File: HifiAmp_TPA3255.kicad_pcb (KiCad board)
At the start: 4 copper layers, 200 x 150 mm, 124 parts, among them J1 PVDD 48V IN — NEEDS_DATA, J2 RCA L SE, J3 RCA R SE, J301 SPK_L, J302 SPK_R, J4 VOLUME_REMOTE, Q301 IPP330P10NM, Q302 IXTK200N10L2, U1 LM5010ASD, U2 LM2940IMP-12/NOPB, U3 TLV1117-33IDCY, U4 OPA1612AIDR, U5 OPA1612AIDR, U6 TPA3255B, U7 TPS3802K33DCKR, U8 LM5069-2

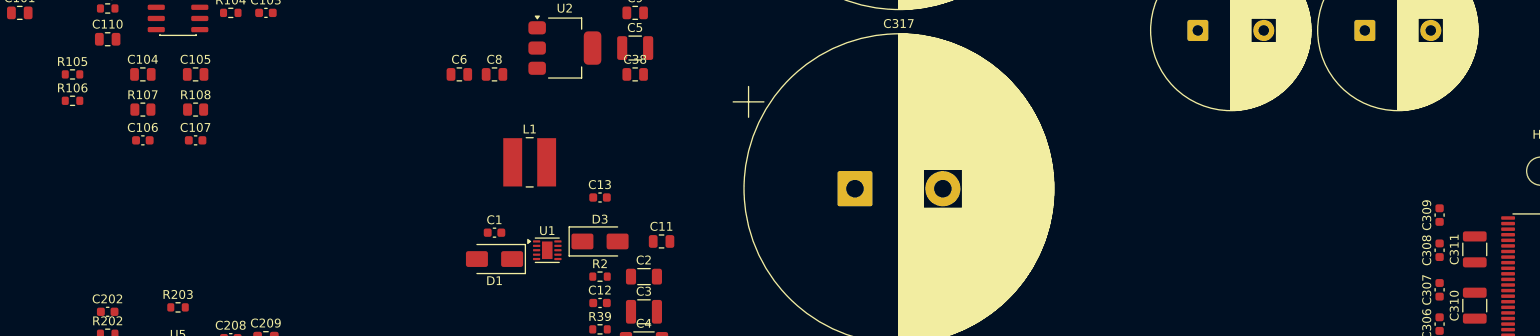
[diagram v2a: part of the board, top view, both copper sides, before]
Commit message: feat(e1.5): correct the two gratuitous asymmetries, and leave the third alone
The mirror around y=175 makes summed ordinates the criterion, not distance, so
C306 and C307 stay put and set the target their partners move to. C308, C309 and
C311 now sum to 350; R105/R106 keep the shared VMID divider but sit midway
between the channels, equalising both reference paths. The inductors' offset is
left as it is: the 2x2 grid is forced by the courtyard, and the mismatch leaves
as an F1 routing constraint instead.

Five IPC moves, all in y. DRC reads 105 violations, every one silkscreen, with
no clearance and no courtyards_overlap — which is what validates the tightest
3.0 mm pitch, since a hand-rolled courtyard calculation would only have proved
its own model. The 119 other footprints are untouched.

The previous session's GUI block is resolved and the escape route verified: the
SendInput block never reached the IPC, and did not survive the session.

Co-Authored-By: Claude Opus 5 <noreply@anthropic.com>
Claude-Session: https://claude.ai/code/session_017KEKgkQHHQWX4vViqUxNCh
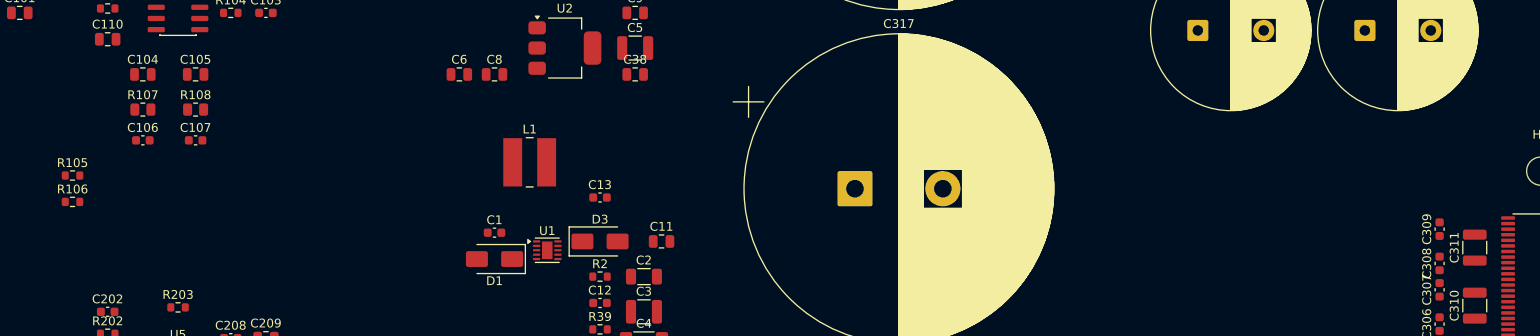
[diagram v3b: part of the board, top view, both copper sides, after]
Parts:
- moved R105 11.5 mm to (118.0, 163.5)
- moved R106 11.5 mm to (118.0, 166.5)
- moved C309 1.60 mm to (273.5, 169.6)
- moved C308 1.50 mm to (273.5, 173.5)
- moved C311 0.20 mm to (277.5, 171.7)
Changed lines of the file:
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@@
 	(footprint "Resistor_SMD:R_0603_1608Metric"
 		(layer "F.Cu")
-		(at 118 155)
+		(at 118 166.5)
 		(descr "Resistor SMD 0603 (1608 Metric), square (rectangular) end terminal, IPC-7351 nominal, (Body size source: IPC-SM-782 page 72, https://www.pcb-3d.com/wordpress/wp-content/uploads/ipc-sm-782a_amendment_1_and_2.pdf)")
 		(tags "resistor")
@@
 	(footprint "Capacitor_SMD:C_0603_1608Metric"
 		(layer "F.Cu")
-		(at 273.5 168 90)
+		(at 273.5 169.6 90)
 		(descr "Capacitor SMD 0603 (1608 Metric), square (rectangular) end terminal, IPC-7351 nominal, (Body size source: IPC-SM-782 page 76, https://www.pcb-3d.com/wordpress/wp-content/uploads/ipc-sm-782a_amendment_1_and_2.pdf)")
 		(tags "capacitor")
@@
 	(footprint "Resistor_SMD:R_0603_1608Metric"
 		(layer "F.Cu")
-		(at 118 152)
+		(at 118 163.5)
 		(descr "Resistor SMD 0603 (1608 Metric), square (rectangular) end terminal, IPC-7351 nominal, (Body size source: IPC-SM-782 page 72, https://www.pcb-3d.com/wordpress/wp-content/uploads/ipc-sm-782a_amendment_1_and_2.pdf)")
 		(tags "resistor")
@@
 	(footprint "Capacitor_SMD:C_0603_1608Metric"
 		(layer "F.Cu")
-		(at 273.5 172 90)
+		(at 273.5 173.5 90)
 		(descr "Capacitor SMD 0603 (1608 Metric), square (rectangular) end terminal, IPC-7351 nominal, (Body size source: IPC-SM-782 page 76, https://www.pcb-3d.com/wordpress/wp-content/uploads/ipc-sm-782a_amendment_1_and_2.pdf)")
 		(tags "capacitor")
@@
 	(footprint "Capacitor_SMD:C_1210_3225Metric"
 		(layer "F.Cu")
-		(at 277.5 171.9 90)
+		(at 277.5 171.7 90)
 		(descr "Capacitor SMD 1210 (3225 Metric), square (rectangular) end terminal, IPC-7351 nominal, (Body size source: IPC-SM-782 page 76, https://www.pcb-3d.com/wordpress/wp-content/uploads/ipc-sm-782a_amendment_1_and_2.pdf)")
 		(tags "capacitor")

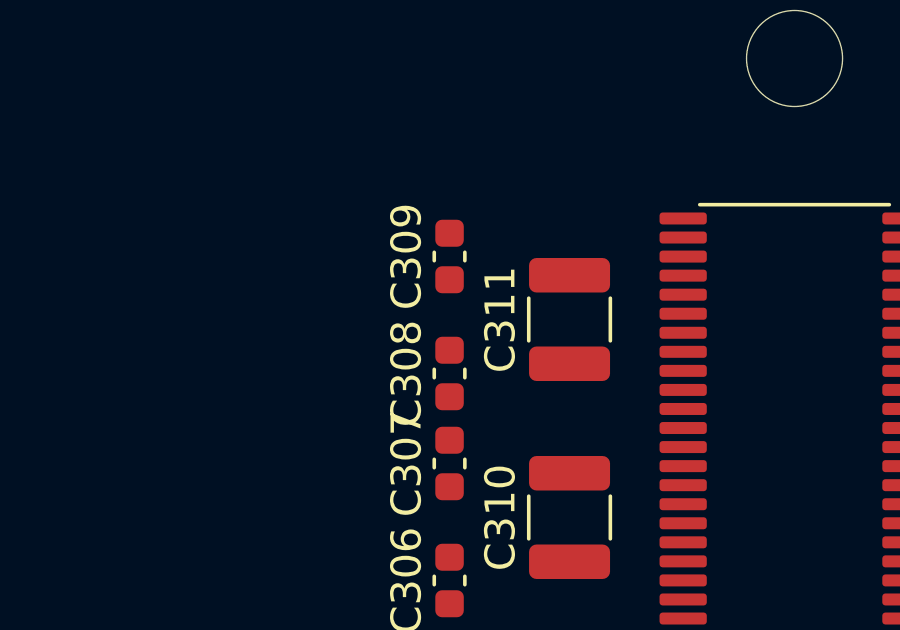
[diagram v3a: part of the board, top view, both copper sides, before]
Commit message: feat(e1.5): finish the mirror by rotating the two reversed bootstraps
C308 and C309 go from 90 to 270 degrees with no move at all: the centres stay
identical to the micron, so the sums to 350 from the corrective slice survive
untouched. C306 and C307 stay as they are — rotating them would cross them.

The crossing test replayed over the six capacitors around U6 now returns zero
crossings, so no bootstrap loop needs a via. DRC holds at silkscreen only, with
no clearance and no courtyards_overlap.

Worth knowing for later checks: the IPC writes this orientation as -90 rather
than 270. Equivalent modulo 360, but a check looking for the literal 270 would
report a failure that is not there.

Co-Authored-By: Claude Opus 5 <noreply@anthropic.com>
Claude-Session: https://claude.ai/code/session_017KEKgkQHHQWX4vViqUxNCh
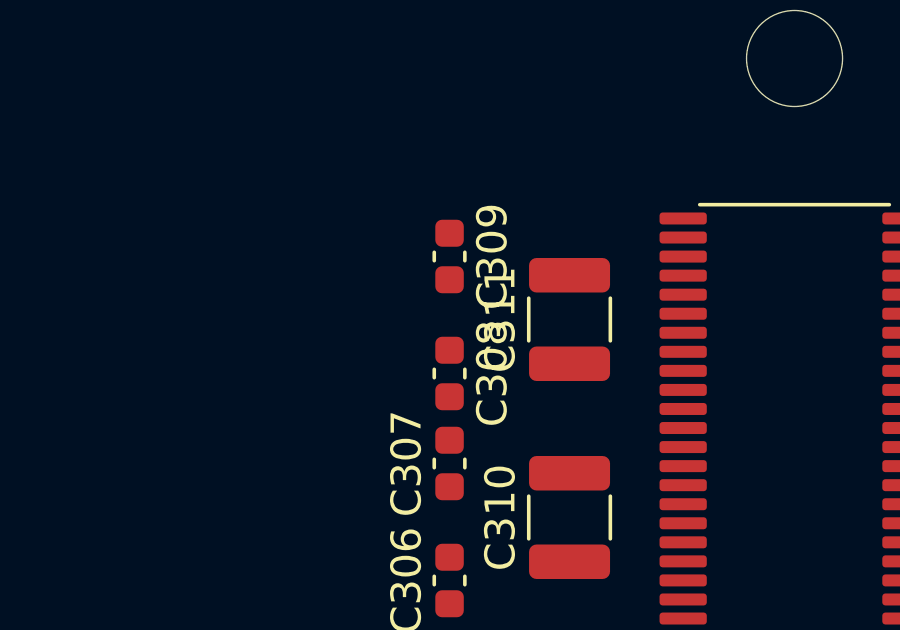
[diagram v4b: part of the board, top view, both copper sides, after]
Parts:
- turned C308 to -90 degrees
- turned C309 to -90 degrees
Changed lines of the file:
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@@
 	(footprint "Capacitor_SMD:C_0603_1608Metric"
 		(layer "F.Cu")
-		(at 273.5 169.6 90)
+		(at 273.5 169.6 -90)
 		(descr "Capacitor SMD 0603 (1608 Metric), square (rectangular) end terminal, IPC-7351 nominal, (Body size source: IPC-SM-782 page 76, https://www.pcb-3d.com/wordpress/wp-content/uploads/ipc-sm-782a_amendment_1_and_2.pdf)")
 		(tags "capacitor")
 		(property "Reference" "C309"
-			(at 0 -1.43 90)
+			(at 0 -1.43 -90)
 			(layer "F.SilkS")
 			(effects
@@
 		)
 		(property "Value" "0.033uF"
-			(at 0 1.43 90)
+			(at 0 1.43 -90)
 			(layer "F.Fab")
 			(effects
@@
 		)
 		(property "Datasheet" ""
-			(at 0 0 90)
+			(at 0 0 -90)
 			(layer "F.Fab")
 			(hide yes)
@@
 		)
 		(property "Description" ""
-			(at 0 0 90)
+			(at 0 0 -90)
 			(layer "F.Fab")
 			(hide yes)
@@
 		)
 		(property "KiLib_Generator" "SMD_2terminal_chip_molded"
-			(at 0 0 90)
+			(at 0 0 -90)
 			(layer "F.SilkS")
 			(hide yes)
@@
 		(duplicate_pad_numbers_are_jumpers no)
 		(fp_line
-			(start -0.14058 -0.51)
-			(end 0.14058 -0.51)
+			(start -0.14058 0.51)
+			(end 0.14058 0.51)
 			(stroke
 				(width 0.12)
@@
 		)
 		(fp_line
-			(start -0.14058 0.51)
-			(end 0.14058 0.51)
+			(start -0.14058 -0.51)
+			(end 0.14058 -0.51)
 			(stroke
 				(width 0.12)
@@
 		)
 		(fp_text user "${REFERENCE}"
-			(at 0 0 90)
+			(at 0 0 -90)
 			(layer "F.Fab")
 			(effects
@@
 		)
 		(pad "1" smd roundrect
-			(at -0.775 0 90)
+			(at -0.775 0 270)
 			(size 0.9 0.95)
 			(layers "F.Cu" "F.Mask" "F.Paste")
@@
 		)
 		(pad "2" smd roundrect
-			(at 0.775 0 90)
+			(at 0.775 0 270)
 			(size 0.9 0.95)
 			(layers "F.Cu" "F.Mask" "F.Paste")
@@
 	(footprint "Capacitor_SMD:C_0603_1608Metric"
 		(layer "F.Cu")
-		(at 273.5 173.5 90)
+		(at 273.5 173.5 -90)
 		(descr "Capacitor SMD 0603 (1608 Metric), square (rectangular) end terminal, IPC-7351 nominal, (Body size source: IPC-SM-782 page 76, https://www.pcb-3d.com/wordpress/wp-content/uploads/ipc-sm-782a_amendment_1_and_2.pdf)")
 		(tags "capacitor")
 		(property "Reference" "C308"
-			(at 0 -1.43 90)
+			(at 0 -1.43 -90)
 			(layer "F.SilkS")
 			(effects
@@
 		)
 		(property "Value" "0.033uF"
-			(at 0 1.43 90)
+			(at 0 1.43 -90)
 			(layer "F.Fab")
 			(effects
@@
 		)
 		(property "Datasheet" ""
-			(at 0 0 90)
+			(at 0 0 -90)
 			(layer "F.Fab")
 			(hide yes)
@@
 		)
 		(property "Description" ""
-			(at 0 0 90)
+			(at 0 0 -90)
 			(layer "F.Fab")
 			(hide yes)
@@
 		)
 		(property "KiLib_Generator" "SMD_2terminal_chip_molded"
-			(at 0 0 90)
+			(at 0 0 -90)
 			(layer "F.SilkS")
 			(hide yes)
@@
 		(duplicate_pad_numbers_are_jumpers no)
 		(fp_line
-			(start -0.14058 -0.51)
-			(end 0.14058 -0.51)
+			(start -0.14058 0.51)
+			(end 0.14058 0.51)
 			(stroke
 				(width 0.12)
@@
 		)
 		(fp_line
-			(start -0.14058 0.51)
-			(end 0.14058 0.51)
+			(start -0.14058 -0.51)
+			(end 0.14058 -0.51)
 			(stroke
 				(width 0.12)
@@
 		)
 		(fp_text user "${REFERENCE}"
-			(at 0 0 90)
+			(at 0 0 -90)
 			(layer "F.Fab")
 			(effects
@@
 		)
 		(pad "1" smd roundrect
-			(at -0.775 0 90)
+			(at -0.775 0 270)
 			(size 0.9 0.95)
 			(layers "F.Cu" "F.Mask" "F.Paste")
@@
 		)
 		(pad "2" smd roundrect
-			(at 0.775 0 90)
+			(at 0.775 0 270)
 			(size 0.9 0.95)
 			(layers "F.Cu" "F.Mask" "F.Paste")

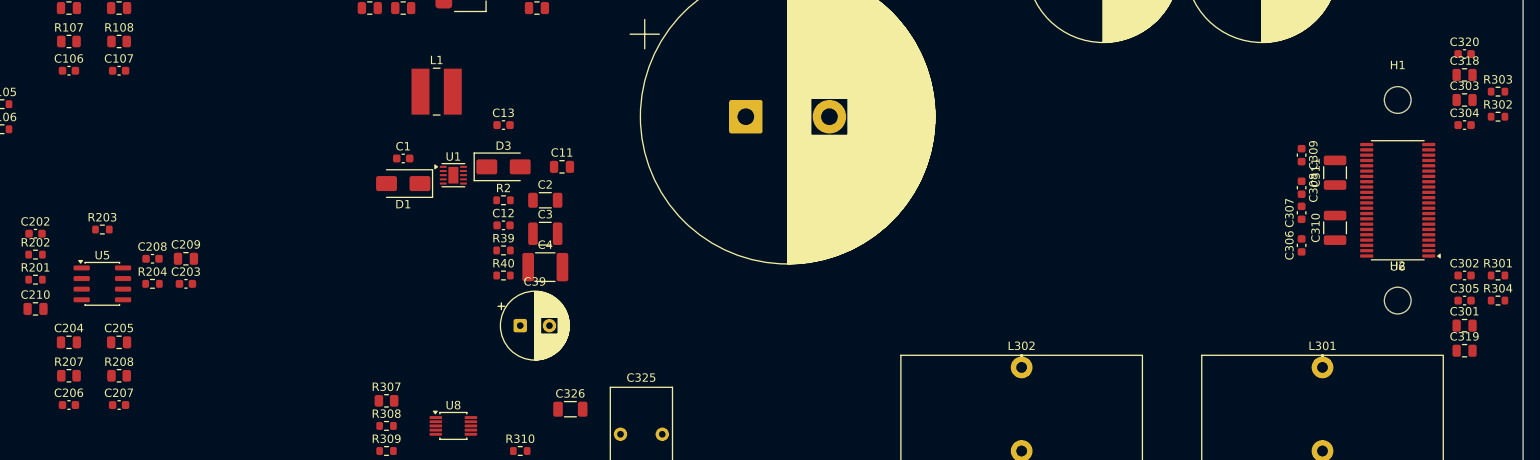
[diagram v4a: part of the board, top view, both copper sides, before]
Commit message: feat(e1.12): move the input capacitors to the load end of a 160 mm run
The four 100 pF anti-aliasing caps now sit 3.5 to 6.5 mm from U6's input pins
instead of 160, with their 100 ohm series resistors left where they were — the
correct topology, and the noise picked up crossing the power zone now shunts to
ground right before the chip rather than never.

The corridor is narrow because the two reserved zones compose: below x=291 the
whole y 160-190 band is closed, and up to x=300 the y 169-181 band is too — and
the input pins land squarely in the second. Only x>=291.5 with y outside
[169,181] was left.

Symmetry is redefined, not lost: these four now follow U6's pinout mirror, with
C106+C207 summing to 350.64 and C107+C206 to 350.63, exactly like the pins they
serve. A check still applying the analog block's (0;+40) would call this broken.

No clearance and no courtyards_overlap, which was the real risk with C302, R301,
C304 and R302 bordering the targets. Silkscreen rises 106 to 112, cosmetic.

Co-Authored-By: Claude Opus 5 <noreply@anthropic.com>
Claude-Session: https://claude.ai/code/session_017KEKgkQHHQWX4vViqUxNCh
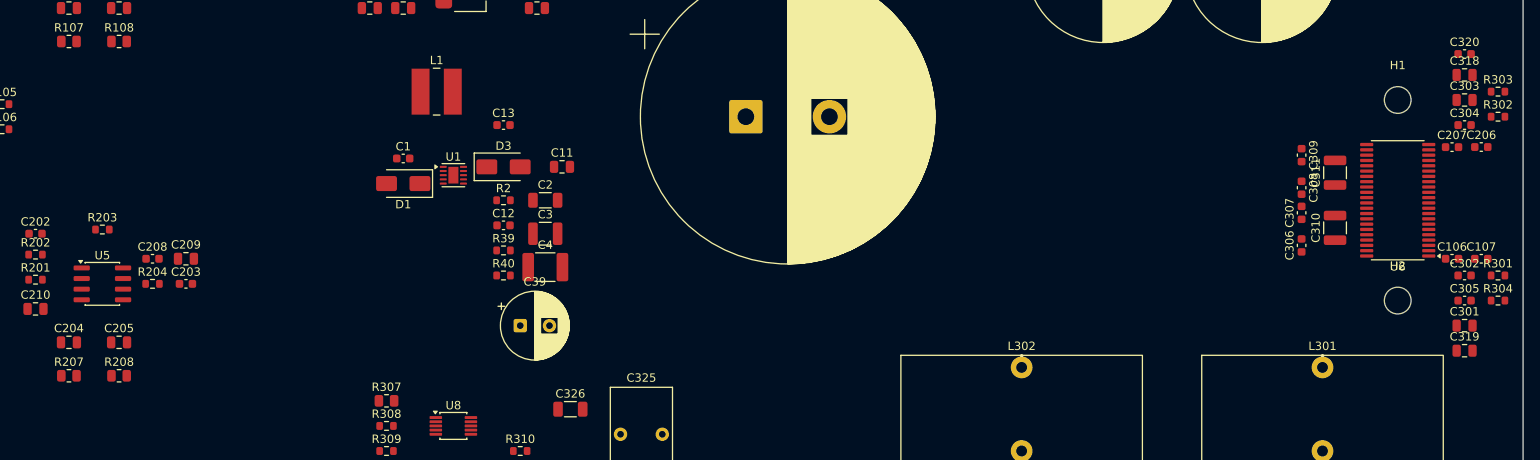
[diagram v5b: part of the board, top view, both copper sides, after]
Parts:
- moved C206 171.8 mm to (295.0, 168.6)
- moved C106 167.0 mm to (291.5, 182.0)
- moved C107 164.5 mm to (295.0, 182.0)
- moved C207 162.5 mm to (291.5, 168.6)
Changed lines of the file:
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@@
 	(footprint "Capacitor_SMD:C_0603_1608Metric"
 		(layer "F.Cu")
-		(at 126 199.5)
+		(at 295 168.63)
 		(descr "Capacitor SMD 0603 (1608 Metric), square (rectangular) end terminal, IPC-7351 nominal, (Body size source: IPC-SM-782 page 76, https://www.pcb-3d.com/wordpress/wp-content/uploads/ipc-sm-782a_amendment_1_and_2.pdf)")
 		(tags "capacitor")
@@
 	(footprint "Capacitor_SMD:C_0603_1608Metric"
 		(layer "F.Cu")
-		(at 126 159.5)
+		(at 291.5 182)
 		(descr "Capacitor SMD 0603 (1608 Metric), square (rectangular) end terminal, IPC-7351 nominal, (Body size source: IPC-SM-782 page 76, https://www.pcb-3d.com/wordpress/wp-content/uploads/ipc-sm-782a_amendment_1_and_2.pdf)")
 		(tags "capacitor")
@@
 	(footprint "Capacitor_SMD:C_0603_1608Metric"
 		(layer "F.Cu")
-		(at 132 199.5)
+		(at 291.5 168.64)
 		(descr "Capacitor SMD 0603 (1608 Metric), square (rectangular) end terminal, IPC-7351 nominal, (Body size source: IPC-SM-782 page 76, https://www.pcb-3d.com/wordpress/wp-content/uploads/ipc-sm-782a_amendment_1_and_2.pdf)")
 		(tags "capacitor")
@@
 	(footprint "Capacitor_SMD:C_0603_1608Metric"
 		(layer "F.Cu")
-		(at 132 159.5)
+		(at 295 182)
 		(descr "Capacitor SMD 0603 (1608 Metric), square (rectangular) end terminal, IPC-7351 nominal, (Body size source: IPC-SM-782 page 76, https://www.pcb-3d.com/wordpress/wp-content/uploads/ipc-sm-782a_amendment_1_and_2.pdf)")
 		(tags "capacitor")

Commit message: feat(e1.11): propagate the pin swap to the board, and close phase E
The swap had been in the schematic since the last session; the board was
behind it. Parity goes from 7 to 3 — the four extra gaps were exactly the
terminal pads — and the intersection test now finds no crossing on either
block, against two before. Nothing else moved: 124 footprints intact to the
micron, pad_prop_heatsink still on U1, lib_footprint_mismatch still 0.

The block was never KiCad's. The RDP session had been disconnected, which
neutralises SendInput for the whole desktop; reconnected, the gesture went
through under automation with no manual step. Worth keeping: activating any
unrelated window still tells the two cases apart in one call.

Two things earned their place in kicad-operations.md. The project manager
opens through explorer.exe on the .kicad_pro, which is what keeps the token
unelevated. And the update dialog ships with "delete footprints with no
symbol" already ticked — on this board that would have destroyed H1 and H2,
the mounting holes that are deliberately symbol-less and that make up two of
the three baseline parity gaps.

The crossing test was calibrated before it was believed: it reports two
crossings on the pre-update file and none after. A first attempt keyed the
source to the output inductor and silently measured nothing, which is the
same empty-proof shape as the schematic_parity zero.

Co-Authored-By: Claude Opus 5 <noreply@anthropic.com>
Claude-Session: https://claude.ai/code/session_019BebeZkXR3UXsLfHa8ZWyd
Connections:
- J301 pad 1: /OUT_A_F -> /OUT_B_F
- J301 pad 2: /OUT_B_F -> /OUT_A_F
- J302 pad 1: /OUT_C_F -> /OUT_D_F
- J302 pad 2: /OUT_D_F -> /OUT_C_F

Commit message: feat(f1.1): route the four bootstrap loops, the board's first copper
Twelve segments on F.Cu, no via — the invariant the whole slice was built
around, and the reason E1.5 removed the last crossing. Unconnected items go
254 to 250, which is what proves the four links actually land on their pads
rather than near them; the 112 silkscreen violations are unchanged and
parity stays at 3.

The GATE_DRIVE class width of 0.5 mm was not usable. U6's pads are
1.575 x 0.4 mm on a 0.635 pitch, leaving 0.435 mm from a track axis to the
neighbouring pad edge: against 0.25 mm clearance, 0.5 gives 0.185 and 0.4
still gives 0.235. 0.35 gives 0.260 and passes. Bootstrap current is
negligible and the board minimum is 0.20, so the narrower track costs
nothing. C310 and C311 sit across the direct runs to C307 and C308; the
1.8 mm gap between their own pads is what BST_B and BST_C thread through.

Two ways a check can lie, both hit here and now written down. A pad offset
rotates by -theta, not +theta: taking +theta swaps the two pads of any
component at +-90 degrees and stays invisible at 0 and 180, so the brief
sent to the router had C306 pad 2 where pad 1 belonged. And "(segment" is
followed by a newline, not a space, so matching "(segment " reports zero
tracks on a routed board without erroring. The DRC settled the first one:
had the tracks ended on the wrong pad, the nets would still read unconnected
and track_dangling would not be zero.

E1.11's crossing proof survives this: every footprint it measured sits at
rotation 0, and U6 at 180, where both conventions agree.

Co-Authored-By: Claude Opus 5 <noreply@anthropic.com>
Claude-Session: https://claude.ai/code/session_019BebeZkXR3UXsLfHa8ZWyd
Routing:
- net /BST_B: track 0.00 -> 10.1 mm
- net /BST_C: track 0.00 -> 10.1 mm
- net /BST_D: track 0.00 -> 7.81 mm
- net /BST_A: track 0.00 -> 7.81 mm
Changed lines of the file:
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@@
 		(layer "Edge.Cuts")
+	)
+	(segment
+		(start 281.2875 168.3325)
+		(end 280 168.3325)
+		(width 0.35)
+		(layer "F.Cu")
+		(net "/BST_D")
+	)
+	(segment
+		(start 280 168.3325)
+		(end 273.5 168.825)
+		(width 0.35)
+		(layer "F.Cu")
+		(net "/BST_D")
+	)
+	(segment
+		(start 279.25 171.7)
+		(end 275.5 171.7)
+		(width 0.35)
+		(layer "F.Cu")
+		(net "/BST_C")
+	)
+	(segment
+		(start 281.2875 168.9675)
+		(end 280 168.9675)
+		(width 0.35)
+		(layer "F.Cu")
+		(net "/BST_C")
+	)
+	(segment
+		(start 275.5 171.7)
+		(end 273.5 172.725)
+		(width 0.35)
+		(layer "F.Cu")
+		(net "/BST_C")
+	)
+	(segment
+		(start 280 168.9675)
+		(end 279.25 171.7)
+		(width 0.35)
+		(layer "F.Cu")
+		(net "/BST_C")
+	)
+	(segment
+		(start 275.5 178.3)
+		(end 273.5 177.275)
+		(width 0.35)
+		(layer "F.Cu")
+		(net "/BST_B")
+	)
+	(segment
+		(start 281.2875 181.0325)
+		(end 280 181.0325)
+		(width 0.35)
+		(layer "F.Cu")
+		(net "/BST_B")
+	)
+	(segment
+		(start 280 181.0325)
+		(end 279.25 178.3)
+		(width 0.35)
+		(layer "F.Cu")
+		(net "/BST_B")
+	)
+	(segment
+		(start 279.25 178.3)
+		(end 275.5 178.3)
+		(width 0.35)
+		(layer "F.Cu")
+		(net "/BST_B")
+	)
+	(segment
+		(start 281.2875 181.6675)
+		(end 280 181.6675)
+		(width 0.35)
+		(layer "F.Cu")
+		(net "/BST_A")
+	)
+	(segment
+		(start 280 181.6675)
+		(end 273.5 181.175)
+		(width 0.35)
+		(layer "F.Cu")
+		(net "/BST_A")
 	)
 	(embedded_fonts no)
